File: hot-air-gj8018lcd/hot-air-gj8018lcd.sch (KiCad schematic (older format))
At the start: 45 parts, among them IC1 ?, T1 BTB06

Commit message: Update hot-air-gj8018lcd.sch
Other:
- moved on the sheet: C5, D10, E1, E2, R3
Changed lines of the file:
@@
 L Diode:1N4007 D10
 U 1 1 5C64632D
-P 6200 1750
-F 0 "D10" H 6246 1671 50  0000 R CNN
-F 1 "?" H 6250 1600 50  0000 R CNN
-F 2 "Diode_THT:D_DO-41_SOD81_P10.16mm_Horizontal" H 6200 1575 50  0001 C CNN
-F 3 "http://www.vishay.com/docs/88503/1n4001.pdf" H 6200 1750 50  0001 C CNN
-	1    6200 1750
+P 6200 1700
+F 0 "D10" H 6246 1621 50  0000 R CNN
+F 1 "?" H 6250 1550 50  0000 R CNN
+F 2 "Diode_THT:D_DO-41_SOD81_P10.16mm_Horizontal" H 6200 1525 50  0001 C CNN
+F 3 "http://www.vishay.com/docs/88503/1n4001.pdf" H 6200 1700 50  0001 C CNN
+	1    6200 1700
 	0    -1   -1   0
 $EndComp
@@
 Connection ~ 7850 1200
 Wire Wire Line
-	7850 1950 7350 1950
-Wire Wire Line
-	7350 1700 7350 1950
-Wire Wire Line
-	7850 1700 7850 1950
+	7850 1900 7350 1900
+Wire Wire Line
+	7350 1700 7350 1900
+Wire Wire Line
+	7850 1700 7850 1900
 $Comp
 L power:GND #PWR?
 U 1 1 5C680120
-P 9000 2100
-F 0 "#PWR?" H 9000 1850 50  0001 C CNN
-F 1 "GND" H 9005 1927 50  0000 C CNN
-F 2 "" H 9000 2100 50  0001 C CNN
-F 3 "" H 9000 2100 50  0001 C CNN
-	1    9000 2100
+P 8950 2050
+F 0 "#PWR?" H 8950 1800 50  0001 C CNN
+F 1 "GND" H 8955 1877 50  0000 C CNN
+F 2 "" H 8950 2050 50  0001 C CNN
+F 3 "" H 8950 2050 50  0001 C CNN
+	1    8950 2050
 	1    0    0    -1
 $EndComp
@@
 	5850 1550 6200 1550
 Wire Wire Line
-	6200 1550 6200 1600
-Wire Wire Line
 	5650 1650 5700 1650
 Wire Wire Line
-	5700 1650 5700 1950
-Wire Wire Line
-	5700 1950 6200 1950
-Wire Wire Line
-	6200 1950 6200 1900
+	5700 1650 5700 1900
+Wire Wire Line
+	5700 1900 6200 1900
 Wire Wire Line
 	5850 1200 6500 1200
@@
 	6500 1200 6500 1400
 Wire Wire Line
-	6500 1700 6500 1950
-Wire Wire Line
-	6500 1950 6200 1950
-Connection ~ 6200 1950
+	6500 1700 6500 1900
+Wire Wire Line
+	6500 1900 6200 1900
 Wire Wire Line
 	6500 1200 7350 1200
 Connection ~ 6500 1200
 Wire Wire Line
-	7000 1700 7000 1950
-Wire Wire Line
-	7000 1950 6500 1950
-Connection ~ 6500 1950
+	7000 1700 7000 1900
+Wire Wire Line
+	7000 1900 6500 1900
+Connection ~ 6500 1900
 Wire Wire Line
 	7000 1400 7000 900
@@
 Wire Wire Line
 	7850 900  7850 1200
-Connection ~ 7850 1950
-Wire Wire Line
-	8550 1700 8550 1950
-Wire Wire Line
-	7850 1950 8200 1950
-Wire Wire Line
-	8200 1950 8200 1700
-Connection ~ 8200 1950
-Wire Wire Line
-	8200 1950 8550 1950
+Connection ~ 7850 1900
+Wire Wire Line
+	8550 1700 8550 1900
+Wire Wire Line
+	7850 1900 8200 1900
+Wire Wire Line
+	8200 1900 8200 1700
+Connection ~ 8200 1900
+Wire Wire Line
+	8200 1900 8550 1900
 Wire Wire Line
 	8200 1400 8200 1200
@@
 L Device:CP C5
 U 1 1 5C6DE2D9
-P 9000 1550
-F 0 "C5" V 8882 1504 50  0000 R CNN
-F 1 "100µF/35V" V 8800 1800 50  0000 R CNN
-F 2 "" H 9038 1400 50  0001 C CNN
-F 3 "~" H 9000 1550 50  0001 C CNN
-	1    9000 1550
+P 8950 1550
+F 0 "C5" V 8832 1504 50  0000 R CNN
+F 1 "100µF/35V" V 8750 1800 50  0000 R CNN
+F 2 "" H 8988 1400 50  0001 C CNN
+F 3 "~" H 8950 1550 50  0001 C CNN
+	1    8950 1550
 	-1   0    0    -1
 $EndComp
 Wire Wire Line
-	8550 1200 9000 1200
-Wire Wire Line
-	9000 1200 9000 1400
+	8550 1200 8950 1200
+Wire Wire Line
+	8950 1200 8950 1400
 Connection ~ 8550 1200
 Wire Wire Line
-	8550 1950 9000 1950
-Wire Wire Line
-	9000 1950 9000 1700
-Connection ~ 8550 1950
+	8550 1900 8950 1900
+Wire Wire Line
+	8950 1900 8950 1700
+Connection ~ 8550 1900
 $Comp
 L power:VCC #PWR?
 U 1 1 5C6E801D
-P 9000 1050
-F 0 "#PWR?" H 9000 900 50  0001 C CNN
-F 1 "VCC" H 9017 1223 50  0000 C CNN
-F 2 "" H 9000 1050 50  0001 C CNN
-F 3 "" H 9000 1050 50  0001 C CNN
-	1    9000 1050
-	1    0    0    -1
-$EndComp
-Wire Wire Line
-	9000 1050 9000 1200
-Connection ~ 9000 1200
-Wire Wire Line
-	9000 1950 9000 2100
-Connection ~ 9000 1950
+P 8950 1050
+F 0 "#PWR?" H 8950 900 50  0001 C CNN
+F 1 "VCC" H 8967 1223 50  0000 C CNN
+F 2 "" H 8950 1050 50  0001 C CNN
+F 3 "" H 8950 1050 50  0001 C CNN
+	1    8950 1050
+	1    0    0    -1
+$EndComp
+Wire Wire Line
+	8950 1050 8950 1200
+Connection ~ 8950 1200
+Wire Wire Line
+	8950 1900 8950 2050
+Connection ~ 8950 1900
 Wire Wire Line
 	3100 2700 3100 2650
@@
 L Device:R R3
 U 1 1 5C707ED9
-P 9400 3850
-F 0 "R3" H 9470 3896 50  0000 L CNN
-F 1 "10K" H 9470 3805 50  0000 L CNN
-F 2 "" V 9330 3850 50  0001 C CNN
-F 3 "~" H 9400 3850 50  0001 C CNN
-	1    9400 3850
-	1    0    0    -1
-$EndComp
-Wire Wire Line
-	8500 3550 8950 3550
-Wire Wire Line
-	9400 3550 9400 3700
+P 9300 3850
+F 0 "R3" H 9370 3896 50  0000 L CNN
+F 1 "10K" H 9370 3805 50  0000 L CNN
+F 2 "" V 9230 3850 50  0001 C CNN
+F 3 "~" H 9300 3850 50  0001 C CNN
+	1    9300 3850
+	1    0    0    -1
+$EndComp
+Wire Wire Line
+	8500 3550 8900 3550
+Wire Wire Line
+	9300 3550 9300 3700
 Connection ~ 8500 3550
 Wire Wire Line
-	8500 4150 8950 4150
-Wire Wire Line
-	9400 4150 9400 4000
+	8500 4150 8900 4150
+Wire Wire Line
+	9300 4150 9300 4000
 Connection ~ 8500 4150
 $Comp
 L Device:CP E1
 U 1 1 5C70DCF1
-P 8950 3850
-F 0 "E1" V 8832 3804 50  0000 R CNN
-F 1 "10µF/50V" V 8750 4100 50  0000 R CNN
-F 2 "" H 8988 3700 50  0001 C CNN
-F 3 "~" H 8950 3850 50  0001 C CNN
-	1    8950 3850
+P 8900 3850
+F 0 "E1" V 8782 3804 50  0000 R CNN
+F 1 "10µF/50V" V 8700 4100 50  0000 R CNN
+F 2 "" H 8938 3700 50  0001 C CNN
+F 3 "~" H 8900 3850 50  0001 C CNN
+	1    8900 3850
 	-1   0    0    -1
 $EndComp
 Wire Wire Line
-	8950 3700 8950 3550
-Connection ~ 8950 3550
-Wire Wire Line
-	8950 3550 9400 3550
-Wire Wire Line
-	8950 4000 8950 4150
-Connection ~ 8950 4150
-Wire Wire Line
-	8950 4150 9400 4150
+	8900 3700 8900 3550
+Connection ~ 8900 3550
+Wire Wire Line
+	8900 3550 9300 3550
+Wire Wire Line
+	8900 4000 8900 4150
+Connection ~ 8900 4150
+Wire Wire Line
+	8900 4150 9300 4150
 Text Label 7950 3550 2    50   ~ 0
 M+
@@
 L Device:CP E2
 U 1 1 5C7B6BEE
-P 7750 5450
-F 0 "E2" V 7632 5404 50  0000 R CNN
-F 1 "10µF/50V" V 7550 5700 50  0000 R CNN
-F 2 "" H 7788 5300 50  0001 C CNN
-F 3 "~" H 7750 5450 50  0001 C CNN
-	1    7750 5450
+P 7800 5450
+F 0 "E2" V 7682 5404 50  0000 R CNN
+F 1 "10µF/50V" V 7600 5700 50  0000 R CNN
+F 2 "" H 7838 5300 50  0001 C CNN
+F 3 "~" H 7800 5450 50  0001 C CNN
+	1    7800 5450
 	-1   0    0    -1
 $EndComp
 Wire Wire Line
-	7400 5700 7750 5700
-Wire Wire Line
-	7750 5700 7750 5600
+	7400 5700 7800 5700
+Wire Wire Line
+	7800 5700 7800 5600
 Connection ~ 7400 5700
 Wire Wire Line
 	7400 5700 7400 5850
 Wire Wire Line
-	7750 5300 7750 5200
-Wire Wire Line
-	7750 5200 7400 5200
+	7800 5300 7800 5200
+Wire Wire Line
+	7800 5200 7400 5200
 Connection ~ 7400 5200
 Wire Wire Line
 	7400 5200 7400 5300
-Text GLabel 8600 5200 2    50   Input ~ 0
+Text GLabel 8650 5200 2    50   Input ~ 0
 P+
 Text GLabel 8600 5400 2    50   Input ~ 0
@@
 T-
 Wire Wire Line
-	7750 5200 8600 5200
-Connection ~ 7750 5200
+	7800 5200 8650 5200
+Connection ~ 7800 5200
 Wire Wire Line
 	8350 5700 8350 5400
@@
 	8350 5400 8600 5400
 Wire Wire Line
-	7750 5700 8350 5700
-Connection ~ 7750 5700
+	7800 5700 8350 5700
+Connection ~ 7800 5700
 $Comp
 L Isolator:TLP127 U?
@@
 Wire Wire Line
 	5050 3650 5050 5900
+Connection ~ 6200 1900
+Wire Wire Line
+	6200 1900 6200 1850
 $EndSCHEMATC

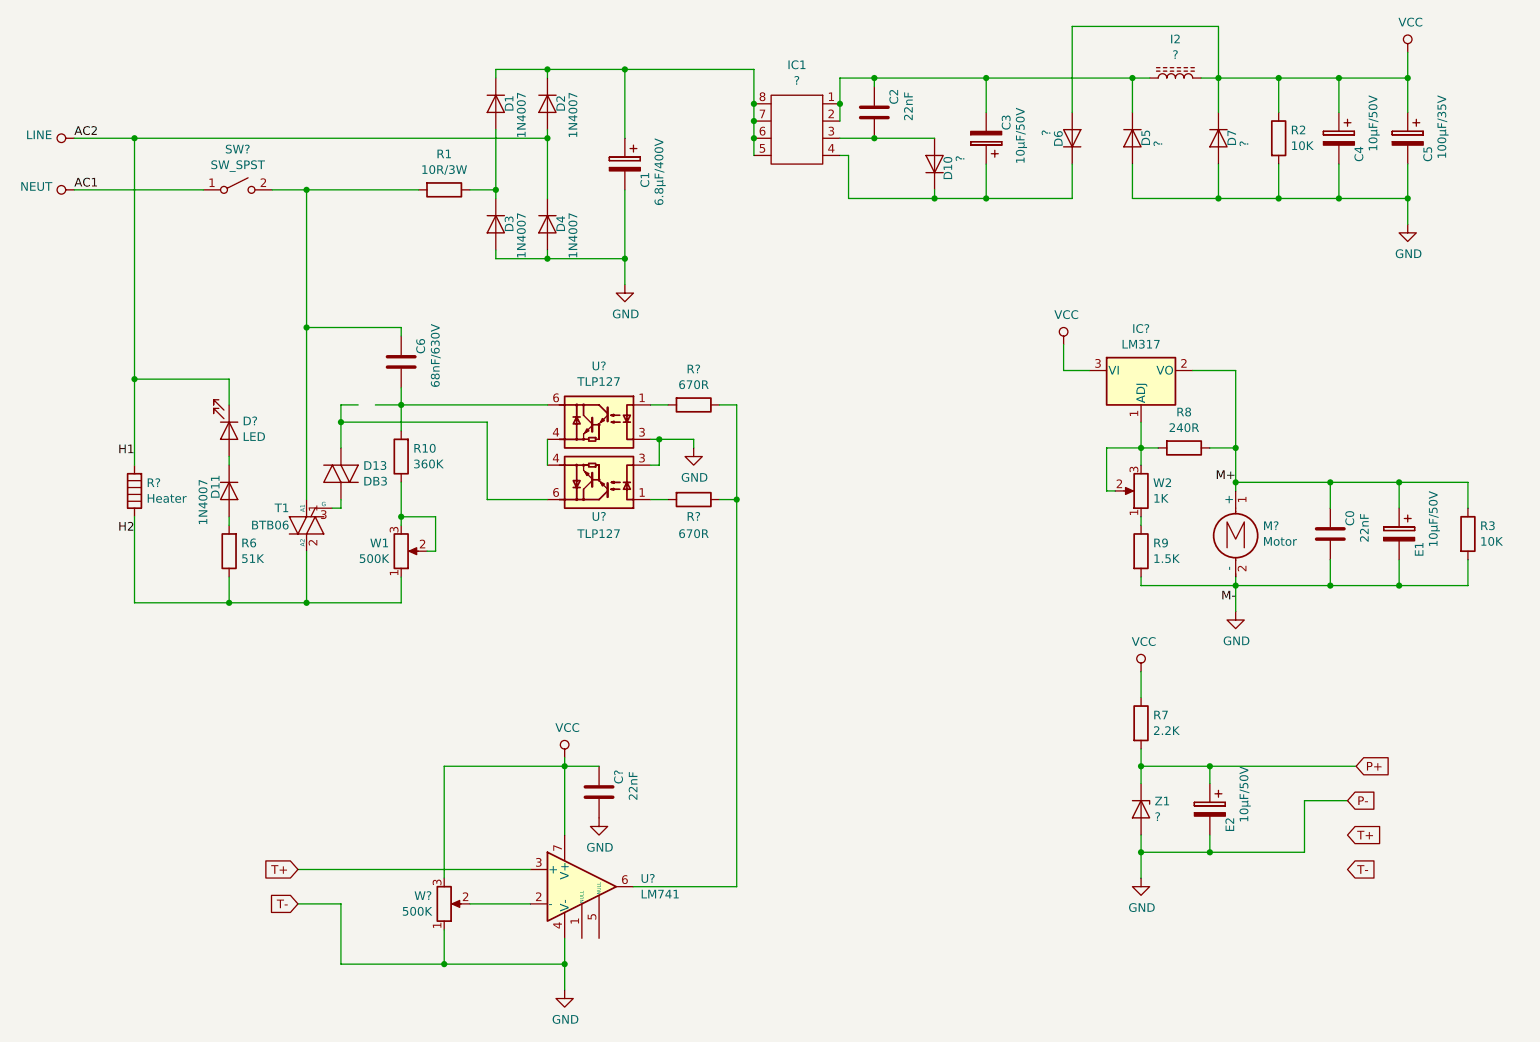
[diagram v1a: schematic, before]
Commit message: Added tooh brush timer schematic
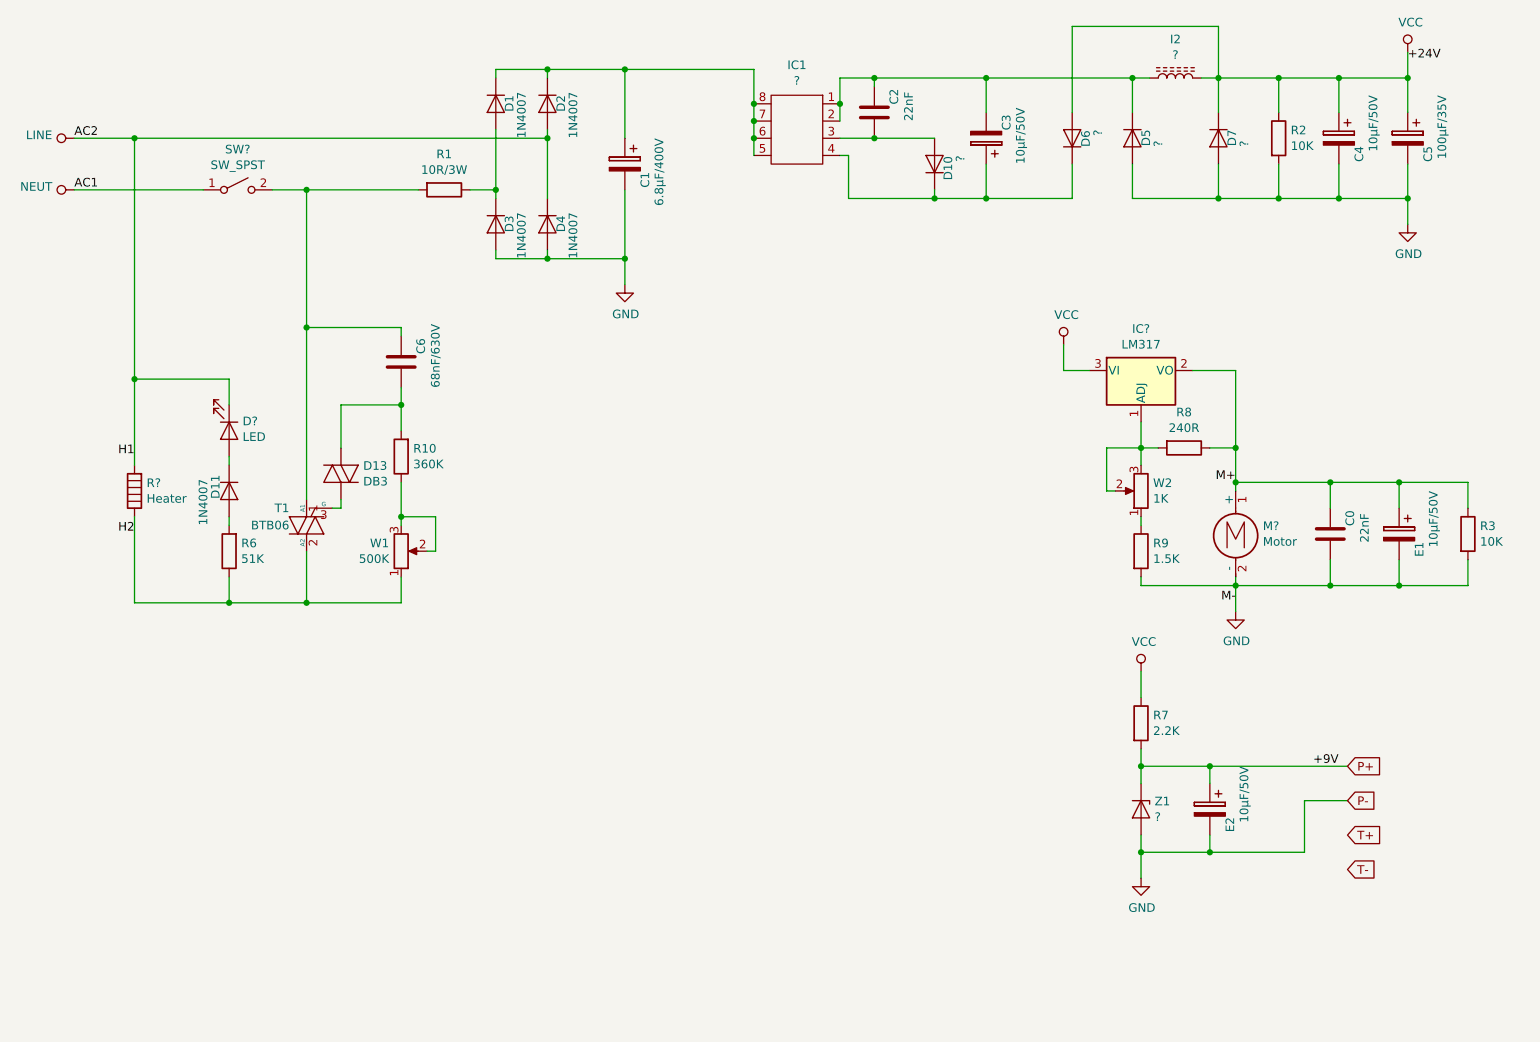
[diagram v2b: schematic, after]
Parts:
- removed C?: 22nF, symbol Device:C
- removed R? (x2): 670R, symbol Device:R
- removed U? (x2): TLP127, Package_SO:MFSOP6-4_4.4x3.6mm_P1.27mm, symbol Isolator:TLP127
- removed U?: LM741, symbol Amplifier_Operational:LM741
- removed W?: 500K, symbol Device:R_POT
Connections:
- net at C6.2, R10.2: now also D13.1 (K)
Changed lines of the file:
@@
 F 3 "http://www.vishay.com/docs/88503/1n4001.pdf" H 7000 1550 50  0001 C CNN
 	1    7000 1550
-	0    1    -1   0
+	0    -1   -1   0
 $EndComp
 $Comp
@@
 Wire Wire Line
 	7400 5200 7400 5300
-Text GLabel 8650 5200 2    50   Input ~ 0
+Text GLabel 8600 5200 2    50   Input ~ 0
 P+
 Text GLabel 8600 5400 2    50   Input ~ 0
@@
 T-
 Wire Wire Line
-	7800 5200 8650 5200
+	7800 5200 8600 5200
 Connection ~ 7800 5200
 Wire Wire Line
@@
 	7800 5700 8350 5700
 Connection ~ 7800 5700
-$Comp
-L Isolator:TLP127 U?
-U 1 1 5C7EFCB2
-P 4250 3550
-F 0 "U?" H 4250 3750 50  0000 C CNN
-F 1 "TLP127" H 4250 3850 50  0000 C CNN
-F 2 "Package_SO:MFSOP6-4_4.4x3.6mm_P1.27mm" H 4250 3250 50  0001 C CIN
-F 3 "https://toshiba.semicon-storage.com/info/docget.jsp?did=16902&prodName=TLP127" H 4180 3550 50  0001 L CNN
-	1    4250 3550
-	-1   0    0    1
-$EndComp
 Wire Wire Line
 	4400 2400 4400 2250
 Connection ~ 4400 2250
-$Comp
-L Isolator:TLP127 U?
-U 1 1 5C7EF88C
-P 4250 3200
-F 0 "U?" H 4250 3525 50  0000 C CNN
-F 1 "TLP127" H 4250 3434 50  0000 C CNN
-F 2 "Package_SO:MFSOP6-4_4.4x3.6mm_P1.27mm" H 4250 2900 50  0001 C CIN
-F 3 "https://toshiba.semicon-storage.com/info/docget.jsp?did=16902&prodName=TLP127" H 4180 3200 50  0001 L CNN
-	1    4250 3200
-	-1   0    0    -1
-$EndComp
-Wire Wire Line
-	3950 3450 3950 3300
-Wire Wire Line
-	4550 3300 4600 3300
-Wire Wire Line
-	4600 3300 4600 3450
-Wire Wire Line
-	4600 3450 4550 3450
-$Comp
-L power:GND #PWR?
-U 1 1 5C83D0DB
-P 4800 3350
-F 0 "#PWR?" H 4800 3100 50  0001 C CNN
-F 1 "GND" H 4805 3177 50  0000 C CNN
-F 2 "" H 4800 3350 50  0001 C CNN
-F 3 "" H 4800 3350 50  0001 C CNN
-	1    4800 3350
-	1    0    0    -1
-$EndComp
-Wire Wire Line
-	4800 3300 4800 3350
-Wire Wire Line
-	4600 3300 4800 3300
-Connection ~ 4600 3300
-$Comp
-L Amplifier_Operational:LM741 U?
-U 1 1 5C84FFE5
-P 4150 5900
-F 0 "U?" H 4491 5946 50  0000 L CNN
-F 1 "LM741" H 4491 5855 50  0000 L CNN
-F 2 "" H 4200 5950 50  0001 C CNN
-F 3 "http://www.ti.com/lit/ds/symlink/lm741.pdf" H 4300 6050 50  0001 C CNN
-	1    4150 5900
-	1    0    0    -1
-$EndComp
-$Comp
-L power:VCC #PWR?
-U 1 1 5C8709AD
-P 4050 5150
-F 0 "#PWR?" H 4050 5000 50  0001 C CNN
-F 1 "VCC" H 4067 5323 50  0000 C CNN
-F 2 "" H 4050 5150 50  0001 C CNN
-F 3 "" H 4050 5150 50  0001 C CNN
-	1    4050 5150
-	1    0    0    -1
-$EndComp
-Wire Wire Line
-	4050 5600 4050 5200
-$Comp
-L power:GND #PWR?
-U 1 1 5C877121
-P 4050 6500
-F 0 "#PWR?" H 4050 6250 50  0001 C CNN
-F 1 "GND" H 4055 6327 50  0000 C CNN
-F 2 "" H 4050 6500 50  0001 C CNN
-F 3 "" H 4050 6500 50  0001 C CNN
-	1    4050 6500
-	1    0    0    -1
-$EndComp
-Wire Wire Line
-	4050 6500 4050 6350
-$Comp
-L Device:C C?
-U 1 1 5C87DB90
-P 4250 5350
-F 0 "C?" V 4365 5396 50  0000 L CNN
-F 1 "22nF" V 4450 5300 50  0000 L CNN
-F 2 "" H 4288 5200 50  0001 C CNN
-F 3 "~" H 4250 5350 50  0001 C CNN
-	1    4250 5350
-	1    0    0    -1
-$EndComp
-Connection ~ 4050 5200
-Wire Wire Line
-	4050 5200 4050 5150
-$Comp
-L power:GND #PWR?
-U 1 1 5C88AF1D
-P 4250 5500
-F 0 "#PWR?" H 4250 5250 50  0001 C CNN
-F 1 "GND" H 4255 5327 50  0000 C CNN
-F 2 "" H 4250 5500 50  0001 C CNN
-F 3 "" H 4250 5500 50  0001 C CNN
-	1    4250 5500
-	1    0    0    -1
-$EndComp
-Wire Wire Line
-	4050 5200 4250 5200
-$Comp
-L Device:R R?
-U 1 1 5C8C719D
-P 4800 3100
-F 0 "R?" V 4593 3100 50  0000 C CNN
-F 1 "670R" V 4684 3100 50  0000 C CNN
-F 2 "" V 4730 3100 50  0001 C CNN
-F 3 "~" H 4800 3100 50  0001 C CNN
-	1    4800 3100
-	0    1    1    0
-$EndComp
-Wire Wire Line
-	5050 5900 4450 5900
-$Comp
-L Device:R_POT W?
-U 1 1 5C916A2E
-P 3350 6000
-F 0 "W?" H 3280 5954 50  0000 R CNN
-F 1 "500K" H 3280 6045 50  0000 R CNN
-F 2 "" H 3350 6000 50  0001 C CNN
-F 3 "~" H 3350 6000 50  0001 C CNN
-	1    3350 6000
-	1    0    0    1
-$EndComp
-Wire Wire Line
-	3350 6150 3350 6350
-Wire Wire Line
-	3350 6350 4050 6350
-Connection ~ 4050 6350
-Wire Wire Line
-	4050 6350 4050 6200
-Wire Wire Line
-	3350 5850 3350 5200
-Wire Wire Line
-	3350 5200 4050 5200
-Wire Wire Line
-	3500 6000 3850 6000
-Text GLabel 2500 5800 0    50   Input ~ 0
-T+
-Text GLabel 2500 6000 0    50   Input ~ 0
-T-
 Connection ~ 1550 2950
 Connection ~ 2550 2650
@@
 Connection ~ 2550 4250
 Wire Wire Line
-	2500 5800 3850 5800
-Wire Wire Line
-	2750 6000 2750 6350
-Wire Wire Line
-	2750 6350 3350 6350
-Connection ~ 3350 6350
-Wire Wire Line
-	2500 6000 2750 6000
-Wire Wire Line
 	2750 3650 2750 3700
-Wire Wire Line
-	2750 3350 2750 3200
-Wire Wire Line
-	2750 3200 3600 3200
-Wire Wire Line
-	3600 3200 3600 3650
-Wire Wire Line
-	3600 3650 3950 3650
-Connection ~ 2750 3200
 Wire Wire Line
 	2550 1850 2550 2650
@@
 	3100 3100 3100 3250
 Wire Wire Line
-	3100 3100 3950 3100
-Wire Wire Line
-	3100 3100 2950 3100
-Wire Wire Line
-	2850 3100 2750 3100
-Wire Wire Line
-	2750 3100 2750 3200
-Wire Wire Line
 	2550 2650 3100 2650
 Wire Wire Line
 	2550 4250 3100 4250
-Wire Wire Line
-	5050 3100 5050 3650
-$Comp
-L Device:R R?
-U 1 1 5CAFFD9B
-P 4800 3650
-F 0 "R?" V 4900 3650 50  0000 C CNN
-F 1 "670R" V 5000 3650 50  0000 C CNN
-F 2 "" V 4730 3650 50  0001 C CNN
-F 3 "~" H 4800 3650 50  0001 C CNN
-	1    4800 3650
-	0    1    1    0
-$EndComp
-Wire Wire Line
-	4550 3650 4650 3650
-Wire Wire Line
-	4950 3650 5050 3650
-Connection ~ 5050 3650
-Wire Wire Line
-	4550 3100 4650 3100
-Wire Wire Line
-	4950 3100 5050 3100
-Wire Wire Line
-	5050 3650 5050 5900
 Connection ~ 6200 1900
 Wire Wire Line
 	6200 1900 6200 1850
+Text Label 8950 1100 0    50   ~ 0
++24V
+Text Label 8400 5200 0    50   ~ 0
++9V
+Wire Wire Line
+	2750 3100 2750 3350
+Wire Wire Line
+	2750 3100 3100 3100
 $EndSCHEMATC
